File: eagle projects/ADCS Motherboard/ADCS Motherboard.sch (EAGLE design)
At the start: 140 parts, among them J1 HDR_10_EZFET_DEBUGGER, J11 CNC_3221-10-0300-00, J3 CNC_3221-10-0300-00, J5 CNC_3221-10-0300-00, J7 TE-1734829-3, J8 CNC_3221-10-0300-00, J9 CNC_3221-14-0300-00, Q1 PMV16XN, Q2 IRLML6246TRPBF, Q3 IRLML2246TRPBF, U1 MSP430F5529IPN, U2 LMV321, U3 ADS7841E_2K5, U4 LMV321, U5 LMV321, U7 HMC1053, Y1 32.768kHz, Y2 CSTCR4M00G15L99, Y3 32.768kHz

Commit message: Replaced connectors for Rev B
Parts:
- removed J8: CNC_3221-10-0300-00, my_library:CNC_3221-10-0300-00
- removed J9: CNC_3221-14-0300-00, my_library:CNC_3221-14-0300-00
- removed R56: 5.1M, rcl:R-US_R0603
- added JP2: (no value), pinhead:PINHD-2X12
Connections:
- removed net N$55: J8.9, R56.2
- removed net RW_X_OUTFG: J9.13, U1.P7.4/TB0.2
- removed net RW_Y_OUTFG: J8.1, U1.P5.7/TB0.1
- removed net RW_Z_OUTFG: J8.2, U1.P3.6/TB0.6
- new net N$1: JP2.24
- new net RW_X_LOCK: JP2.9
- new net RW_Y_LOCK: JP2.15
- new net RW_Z_LOCK: JP2.3
- net !CS!_CURR_SENSE_MTQR: now also JP2.23; no longer J8.5
- net !CS!_CURR_SENSE_RW: now also JP2.21; no longer J8.3
- net ACT_BRD_3V_PRESENT: no longer J8.7
- net ACT_BRD_5V_PRESENT: now also JP2.2; no longer J9.14
- net GND: no longer R56.1
- net MAG_X_FIN: now also JP2.8; no longer J9.10
- net MAG_X_RIN: now also JP2.6; no longer J9.12
- net MAG_Y_FIN: now also JP2.12; no longer J9.6
- net MAG_Y_RIN: now also JP2.10; no longer J9.8
- net MAG_Z_FIN: now also JP2.16; no longer J9.2
- net MAG_Z_RIN: now also JP2.14; no longer J9.4
- net N$57: now also JP2.4; no longer J8.10
- net RW_X_DIR: now also JP2.13; no longer J9.7
- net RW_X_SPEED_CTRL: now also JP2.11; no longer J9.1
- net RW_Y_DIR: now also JP2.19; no longer J9.9
- net RW_Y_SPEED_CTRL: now also JP2.17; no longer J9.3
- net RW_Z_DIR: now also JP2.7; no longer J9.11
- net RW_Z_SPEED_CTRL: now also JP2.5; no longer J9.5
- net UCB0_SPI_CLK: now also JP2.18; no longer J8.4
- net UCB0_SPI_MISO: now also JP2.22; no longer J8.6
- net UCB0_SPI_MOSI: now also JP2.20; no longer J8.8
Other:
- note removed: "PWM_IN"

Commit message: Ton of layout changes.. too many to count but this is rev b
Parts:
- removed JP1: (no value), my_library:PINHD-1X5
- removed R39, R40: 10k, rcl:R-US_R0402
- removed U5: LMV321, my_library:LMV321
- added C32, C33: 0.1uF, rcl:C-EUC0805
- added R57, R58: 5.1M, rcl:R-US_R0402
- added R59, R60: 4.7k, rcl:R-US_R0603
- added U10: TSV991AILT, my_library:TSV991AILT
- added U9: BMX160, my_library:BMX160
- J2, R48, U6, Y3: POPULATE (none) -> DNP
- R19: device rcl:R-US_R0805 -> rcl:R-US_R0402
- U2, U4: value LMV321 -> TSV991AILT; device my_library:LMV321 -> my_library:TSV991AILT
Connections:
- removed net N$57: JP2.4, R55.1
- removed net P1.0: JP1.1, U1.P1.0/TA0CLK/ACLK
- removed net P1.1: JP1.2, U1.P1.1/TA0.0
- removed net P2.3: JP1.3, U1.P2.3/TA2.0
- new net !CS!_SPD_SENSE_RW: JP2.24, U1.P3.6/TB0.6
- new net BMX160_INT1: U1.P2.3/TA2.0, U9.INT1
- new net BMX160_INT2: U9.INT2
- new net N$18: R58.1, U9.DNC_2
- new net N$19: R57.1, U9.DNC_1
- new net N$2: C32.1, U9.VDDIO
- new net N$41: U1.P3.7/TB0OUTH/SVMOUT
- net !CS!_CURR_SENSE_MTQR: now also U1.P5.7/TB0.1; no longer U1.P5.1/A9/VREF-/VEREF-
- net !CS!_CURR_SENSE_RW: now also U1.P7.4/TB0.2; no longer U1.P5.0/A8/VREF+/VEREF+
- net !CS!_HMC1053: now also U1.P7.1/CB9/A13; no longer U1.P2.7/UCB0STE/UCA0CLK
- net !CS!_SUN_X+: now also U1.PJ.2/TMS; no longer U1.P4.3/PM_UCB1CLK/PM_UCA1STE
- net !CS!_SUN_X-: now also U1.P6.0/CB0/A0; no longer U1.P8.0
- net !CS!_SUN_Y+: now also U1.P6.2/CB2/A2; no longer U1.P6.5/CB5/A5
- net !CS!_SUN_Y-: now also U1.P6.3/CB3/A3; no longer U1.P8.1
- net !CS!_SUN_Z+: now also U1.P6.1/CB1/A1; no longer U1.P6.6/CB6/A6
- net !CS!_SUN_Z-: now also U1.PJ.3/TCK; no longer U1.P8.2
- net +3V3: now also C33.1, R59.2, R60.2, U10.VCC, U2.VCC, U4.VCC, U9.VDD; no longer R39.2, R40.2, U2.V+, U4.V+, U5.V+
- net ACT_BRD_3V_PRESENT: now also JP2.1
- net BNO055_INT: now also U1.P2.2/TA2CLK/SMCLK; no longer U1.P1.6/TA1CLK/CBOUT
- net BNO055_RST: now also U1.P7.2/CB10/A14; no longer U1.P6.3/CB3/A3
- net B_MEAS_X: now also U2.OUT; no longer U4.OUT
- net B_MEAS_Y: now also U10.OUT; no longer U2.OUT
- net B_MEAS_Z: now also U4.OUT; no longer U5.OUT
- net GND: now also C32.2, C33.2, R55.1, R57.2, R58.2, U10.VSS, U2.VSS, U4.VSS, U9.CSB, U9.GNDIO, U9.GND_1, U9.GND_2, U9.GND_3, U9.SDO; no longer R55.2, U2.V-, U4.V-, U5.V-
- net HMC1053_RESET: now also U1.P6.5/CB5/A5; no longer U1.P6.4/CB4/A4
- net MAG_X_FIN: now also U1.P1.3/TA0.2; no longer U1.P1.2/TA0.1
- net MAG_X_RIN: now also U1.P1.2/TA0.1; no longer U1.P1.3/TA0.2
- net MAG_Y_FIN: now also U1.P1.5/TA0.4; no longer U1.P2.0/TA1.1
- net MAG_Y_RIN: now also U1.P1.4/TA0.3; no longer U1.P2.1/TA1.2
- net MAG_Z_FIN: now also U1.P2.1/TA1.2; no longer U1.P1.4/TA0.3
- net MAG_Z_RIN: now also U1.P2.0/TA1.1; no longer U1.P1.5/TA0.4
- net MSP430_ACTIVE: now also U1.P6.4/CB4/A4; no longer U1.P6.0/CB0/A0
- net N$1: now also JP2.4, R55.2; no longer JP2.24
- net N$21: now also U10.IN-; no longer U2.-
- net N$23: now also U10.IN+; no longer U2.+
- net N$50: now also U2.IN-; no longer U4.-
- net N$52: now also U2.IN+; no longer U4.+
- net N$60: now also U4.IN-; no longer U5.-
- net N$62: now also U4.IN+; no longer U5.+
- net RESERVED_1: now also U1.P2.6/RTCCLK/DMAE0; no longer U1.P2.2/TA2CLK/SMCLK
- net RESERVED_2: now also U1.P2.7/UCB0STE/UCA0CLK; no longer U1.P2.6/RTCCLK/DMAE0
- net RW_X_DIR: now also U1.P4.6/PM_NONE; no longer U1.PJ.3/TCK
- net RW_X_LOCK: now also U1.P1.0/TA0CLK/ACLK
- net RW_Y_DIR: now also U1.P4.7/PM_NONE; no longer U1.PJ.2/TMS
- net RW_Y_LOCK: now also U1.P1.1/TA0.0
- net RW_Z_DIR: now also U1.P5.6/TB0.0; no longer U1.PJ.1/TDI/TCLK
- net RW_Z_LOCK: now also U1.P1.6/TA1CLK/CBOUT
- net TB0.3: no longer JP1.4
- net TB0.4: no longer JP1.5
- net UCB1_I2C_SCL: now also R60.1, U9.SCX; no longer R40.1
- net UCB1_I2C_SDA: now also R59.1, U9.SDX; no longer R39.1
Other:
- note added: "BMX160_INT2"
- note added: "COMPONENTS NOT POPULATED ON REV B DUE TO CHIP SHORTAGE"
- note added: "CSB is I2C/SPI mode select pin Set to GND is I2C mode"
- note added: "SDO is address select pin Set to GND address = 0x68"
- note removed: "was !CS!_SUN_Y+"
- note removed: "was !CS!_SUN_Z+"
- moved on the sheet: C24, C25, C26, C27, C28, J2, JP2, LED2, LED3, R30, R31, R32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

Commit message: Rev B almost ready
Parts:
- removed J3: CNC_3221-10-0300-00, my_library:CNC_3221-10-0300-00
- added JP1: (no value), pinhead:PINHD-2X5
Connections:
- net !CS!_SUN_X+: now also JP1.2; no longer J3.2
- net !CS!_SUN_X-: now also JP1.7; no longer J3.7
- net !CS!_SUN_Y+: now also JP1.4; no longer J3.4
- net !CS!_SUN_Y-: now also JP1.9; no longer J3.9
- net !CS!_SUN_Z-: now also JP1.6; no longer J3.6
- net N$58: now also JP1.8; no longer J3.8
- net UCB0_SPI_CLK: now also JP1.5; no longer J3.5
- net UCB0_SPI_MISO: now also JP1.1; no longer J3.1
- net UCB0_SPI_MOSI: now also JP1.3; no longer J3.3
- net Z-_SUN_3V_PRESENT: now also JP1.10; no longer J3.10
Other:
- moved on the sheet: JP4, R45

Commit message: Idk what i changed
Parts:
- Q1: value PMV16XN -> BSR802NL6327HTSA1; device my_library:PMV16XN -> my_library:BSR802NL6327HTSA1
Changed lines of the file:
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@@
 <part name="R36" library="rcl" library_urn="urn:adsk.eagle:library:334" deviceset="R-US_" device="R0603" package3d_urn="urn:adsk.eagle:package:23555/3" value="10k"/>
 <part name="SUPPLY26" library="supply2" library_urn="urn:adsk.eagle:library:372" deviceset="GND" device=""/>
-<part name="Q1" library="my_library" library_urn="urn:adsk.eagle:library:22876504" deviceset="PMV16XN" device="" package3d_urn="urn:adsk.eagle:package:24628515/1"/>
+<part name="Q1" library="my_library" library_urn="urn:adsk.eagle:library:22876504" deviceset="BSR802NL6327HTSA1" device="" package3d_urn="urn:adsk.eagle:package:24628515/1"/>
 <part name="Q3" library="my_library" library_urn="urn:adsk.eagle:library:22876504" deviceset="IRLML2246TRPBF" device="" package3d_urn="urn:adsk.eagle:package:24628516/1"/>
 <part name="Q2" library="my_library" library_urn="urn:adsk.eagle:library:22876504" deviceset="IRLML6246TRPBF" device="" package3d_urn="urn:adsk.eagle:package:24628516/1"/>
@@
 </instance>
 <instance part="Q1" gate="G$1" x="241.3" y="162.56" smashed="yes" rot="MR0">
-<attribute name="VALUE" x="232.41" y="161.29" size="1.778" layer="96" rot="MR0"/>
-<attribute name="NAME" x="232.41" y="163.83" size="1.778" layer="95" rot="MR0"/>
+<attribute name="VALUE" x="245.11" y="166.37" size="1.778" layer="96" rot="MR180"/>
+<attribute name="NAME" x="245.11" y="168.91" size="1.778" layer="95" rot="MR180"/>
 </instance>
 <instance part="FRAME1" gate="G$1" x="0" y="0" smashed="yes"/>
@@
 <wire x1="218.44" y1="170.18" x2="238.76" y2="170.18" width="0.1524" layer="91"/>
 <pinref part="R7" gate="G$1" pin="1"/>
-<wire x1="238.76" y1="170.18" x2="248.92" y2="170.18" width="0.1524" layer="91"/>
 <wire x1="218.44" y1="170.18" x2="218.44" y2="172.72" width="0.1524" layer="91"/>
 <junction x="218.44" y="170.18"/>
@@
 <junction x="218.44" y="160.02"/>
 <wire x1="218.44" y1="160.02" x2="210.82" y2="160.02" width="0.1524" layer="91"/>
-<label x="248.92" y="170.18" size="1.778" layer="95" rot="MR180" xref="yes"/>
+<label x="248.92" y="175.26" size="1.778" layer="95" rot="MR180" xref="yes"/>
 <pinref part="S1" gate="1" pin="S1"/>
 <wire x1="208.28" y1="160.02" x2="210.82" y2="160.02" width="0.1524" layer="91"/>
@@
 <pinref part="Q1" gate="G$1" pin="D"/>
 <junction x="238.76" y="170.18"/>
-</segment>
-</net>
+<wire x1="238.76" y1="170.18" x2="238.76" y2="175.26" width="0.1524" layer="91"/>
+<wire x1="238.76" y1="175.26" x2="248.92" y2="175.26" width="0.1524" layer="91"/>
+</segment>
+</net>

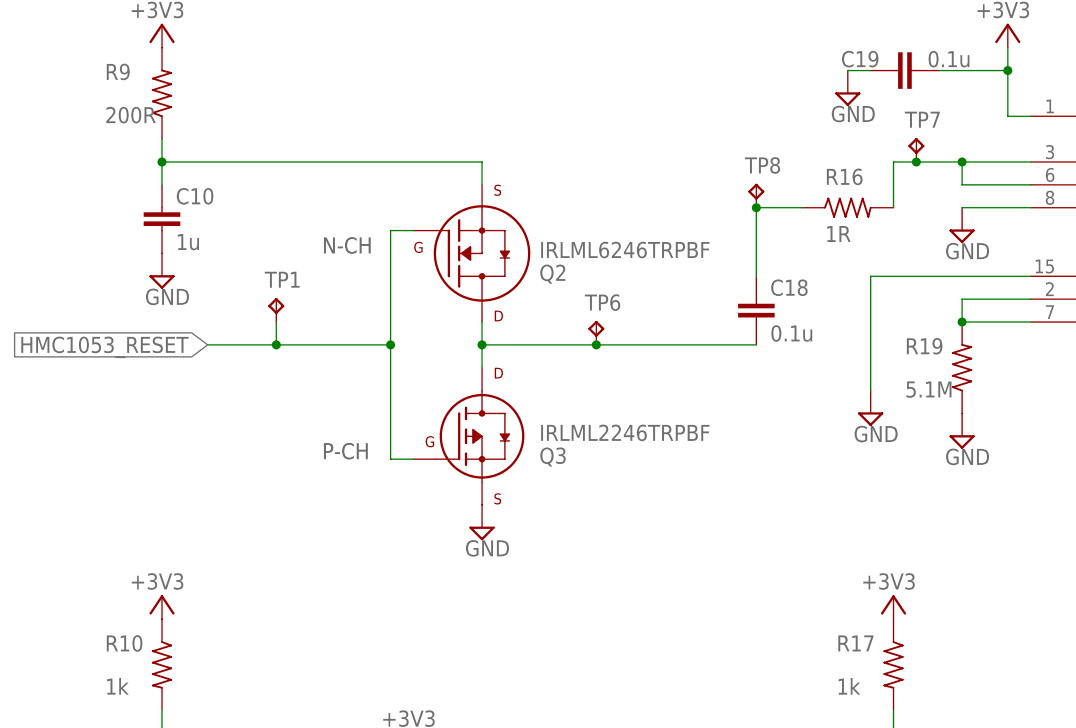
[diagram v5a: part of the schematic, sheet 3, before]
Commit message: Replace totem pole driver with complementary Mosfets pair package
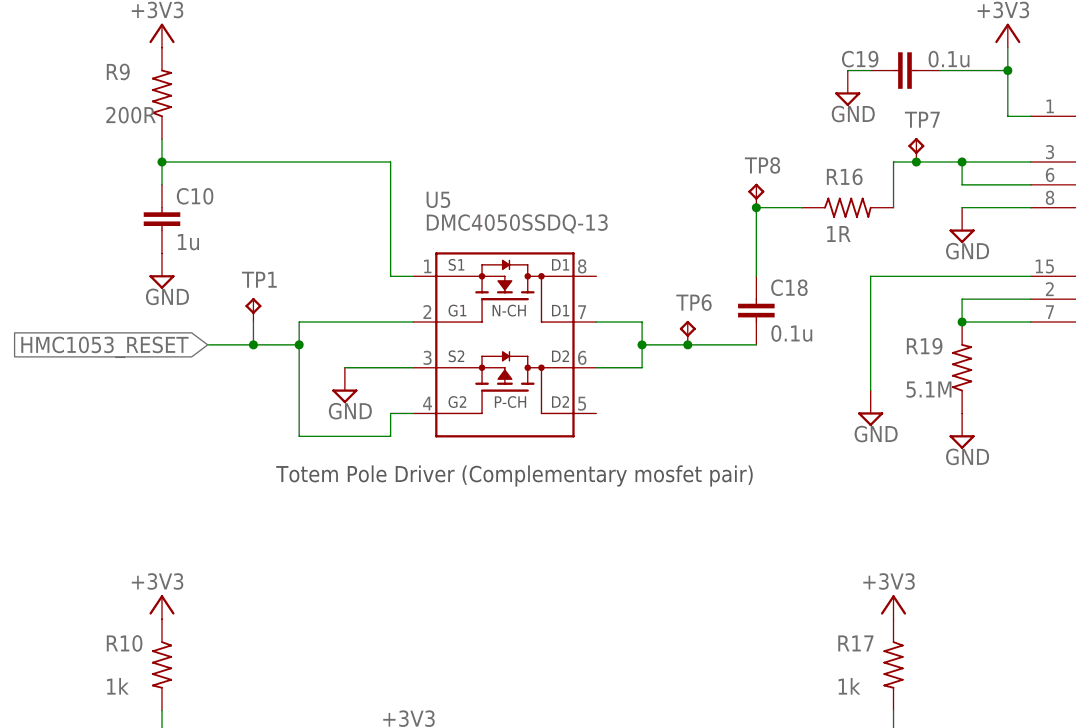
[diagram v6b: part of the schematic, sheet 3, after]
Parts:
- removed Q2: IRLML6246TRPBF, my_library:IRLML6246TRPBF
- removed Q3: IRLML2246TRPBF, my_library:IRLML2246TRPBF
- added U5: DMC4050SSDQ-13, my_library:DMC4050SSDQ-13
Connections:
- net GND: now also U5.S2; no longer Q3.S
- net HMC1053_RESET: now also U5.G1, U5.G2; no longer Q2.G, Q3.G
- net N$39: now also U5.S1; no longer Q2.S
- net N$9: now also U5.D1_2, U5.D2_1; no longer Q2.D, Q3.D
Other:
- note added: "Totem Pole Driver (Complementary mosfet pair)"
- note removed: "N-CH"
- note removed: "P-CH"
- moved on the sheet: TP1, TP6
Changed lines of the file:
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@@
 <part name="SUPPLY26" library="supply2" library_urn="urn:adsk.eagle:library:372" deviceset="GND" device=""/>
 <part name="Q1" library="my_library" library_urn="urn:adsk.eagle:library:22876504" deviceset="BSR802NL6327HTSA1" device="" package3d_urn="urn:adsk.eagle:package:24628515/1"/>
-<part name="Q3" library="my_library" library_urn="urn:adsk.eagle:library:22876504" deviceset="IRLML2246TRPBF" device="" package3d_urn="urn:adsk.eagle:package:24628516/1"/>
-<part name="Q2" library="my_library" library_urn="urn:adsk.eagle:library:22876504" deviceset="IRLML6246TRPBF" device="" package3d_urn="urn:adsk.eagle:package:24628516/1"/>
 <part name="+3V2" library="supply1" deviceset="+3V3" device=""/>
 <part name="J4" library="my_library" library_urn="urn:adsk.eagle:library:22876504" deviceset="HDR_1X2" device="_" package3d_urn="urn:adsk.eagle:package:24527019/1"/>
@@
 <part name="U4" library="my_library" library_urn="urn:adsk.eagle:library:22876504" deviceset="TSV991AILT" device="" package3d_urn="urn:adsk.eagle:package:24426275/2"/>
 <part name="JP1" library="pinhead" library_urn="urn:adsk.eagle:library:325" deviceset="PINHD-2X5" device="" package3d_urn="urn:adsk.eagle:package:22470/2"/>
+<part name="U5" library="my_library" library_urn="urn:adsk.eagle:library:22876504" deviceset="DMC4050SSDQ-13" device=""/>
 </parts>
 <sheets>
@@
 BUSY - Output high impedance when !CS! is HIGH</text>
 <text x="119.38" y="17.78" size="1.778" layer="97">NC</text>
-<text x="45.72" y="154.94" size="1.778" layer="97">P-CH</text>
-<text x="45.72" y="177.8" size="1.778" layer="97">N-CH</text>
 <text x="261.62" y="7.62" size="2.54" layer="94">A.1</text>
+<text x="40.64" y="152.4" size="1.778" layer="97">Totem Pole Driver (Complementary mosfet pair)</text>
 </plain>
 <instances>
@@
 <attribute name="VALUE" x="102.235" y="192.405" size="1.778" layer="96"/>
 </instance>
-<instance part="SUPPLY54" gate="GND" x="63.5" y="147.32" smashed="yes">
-<attribute name="VALUE" x="61.595" y="144.145" size="1.778" layer="96"/>
+<instance part="SUPPLY54" gate="GND" x="48.26" y="162.56" smashed="yes">
+<attribute name="VALUE" x="46.355" y="159.385" size="1.778" layer="96"/>
 </instance>
 <instance part="+3V24" gate="G$1" x="27.94" y="203.2" smashed="yes">
@@
 <attribute name="VALUE" x="199.39" y="113.538" size="1.778" layer="96"/>
 </instance>
-<instance part="TP1" gate="G$1" x="40.64" y="172.72" smashed="yes">
-<attribute name="NAME" x="39.37" y="173.99" size="1.778" layer="95"/>
+<instance part="TP1" gate="G$1" x="38.1" y="172.72" smashed="yes">
+<attribute name="NAME" x="36.83" y="173.99" size="1.778" layer="95"/>
 </instance>
 <instance part="TP2" gate="G$1" x="147.32" y="43.18" smashed="yes">
 <attribute name="NAME" x="146.05" y="44.45" size="1.778" layer="95"/>
-</instance>
-<instance part="Q3" gate="G$1" x="60.96" y="157.48" smashed="yes" rot="MR180">
-<attribute name="VALUE" x="69.85" y="158.75" size="1.778" layer="96" rot="MR180"/>
-<attribute name="NAME" x="69.85" y="156.21" size="1.778" layer="95" rot="MR180"/>
-</instance>
-<instance part="Q2" gate="G$1" x="60.96" y="177.8" smashed="yes" rot="MR180">
-<attribute name="VALUE" x="69.85" y="179.07" size="1.778" layer="96" rot="MR180"/>
-<attribute name="NAME" x="69.85" y="176.53" size="1.778" layer="95" rot="MR180"/>
 </instance>
 <instance part="FRAME2" gate="G$1" x="0" y="0" smashed="yes"/>
@@
 <attribute name="VALUE" x="104.775" y="156.845" size="1.778" layer="96"/>
 </instance>
-<instance part="TP6" gate="G$1" x="76.2" y="170.18" smashed="yes">
-<attribute name="NAME" x="74.93" y="171.45" size="1.778" layer="95"/>
+<instance part="TP6" gate="G$1" x="86.36" y="170.18" smashed="yes">
+<attribute name="NAME" x="85.09" y="171.45" size="1.778" layer="95"/>
 </instance>
 <instance part="TP7" gate="G$1" x="111.76" y="190.5" smashed="yes">
@@
 <attribute name="NAME" x="226.06" y="102.87" size="1.27" layer="95"/>
 <attribute name="VALUE" x="226.06" y="100.33" size="1.27" layer="96"/>
+</instance>
+<instance part="U5" gate="G$1" x="63.5" y="167.64" smashed="yes">
+<attribute name="VALUE" x="57.15" y="180.34" size="1.778" layer="96"/>
+<attribute name="NAME" x="57.15" y="182.88" size="1.778" layer="95"/>
 </instance>
 </instances>
@@
 </segment>
 <segment>
-<pinref part="SUPPLY54" gate="GND" pin="GND"/>
-<pinref part="Q3" gate="G$1" pin="S"/>
-</segment>
-<segment>
 <pinref part="C29" gate="G$1" pin="2"/>
 <pinref part="SUPPLY40" gate="GND" pin="GND"/>
@@
 <pinref part="SUPPLY34" gate="GND" pin="GND"/>
 <wire x1="220.98" y1="86.36" x2="220.98" y2="83.82" width="0.1524" layer="91"/>
+</segment>
+<segment>
+<pinref part="U5" gate="G$1" pin="S2"/>
+<pinref part="SUPPLY54" gate="GND" pin="GND"/>
+<wire x1="55.88" y1="165.1" x2="48.26" y2="165.1" width="0.1524" layer="91"/>
 </segment>
 </net>
@@
 <net name="HMC1053_RESET" class="0">
 <segment>
-<wire x1="53.34" y1="167.64" x2="40.64" y2="167.64" width="0.1524" layer="91"/>
-<wire x1="40.64" y1="170.18" x2="40.64" y2="167.64" width="0.1524" layer="91"/>
-<junction x="40.64" y="167.64"/>
-<wire x1="40.64" y1="167.64" x2="33.02" y2="167.64" width="0.1524" layer="91"/>
+<wire x1="43.18" y1="167.64" x2="38.1" y2="167.64" width="0.1524" layer="91"/>
+<wire x1="38.1" y1="170.18" x2="38.1" y2="167.64" width="0.1524" layer="91"/>
+<junction x="38.1" y="167.64"/>
+<wire x1="38.1" y1="167.64" x2="33.02" y2="167.64" width="0.1524" layer="91"/>
 <label x="33.02" y="167.64" size="1.778" layer="95" rot="R180" xref="yes"/>
 <pinref part="TP1" gate="G$1" pin="TP"/>
-<pinref part="Q3" gate="G$1" pin="G"/>
-<wire x1="55.88" y1="154.94" x2="53.34" y2="154.94" width="0.1524" layer="91"/>
-<pinref part="Q2" gate="G$1" pin="G"/>
-<wire x1="53.34" y1="154.94" x2="53.34" y2="167.64" width="0.1524" layer="91"/>
-<wire x1="53.34" y1="167.64" x2="53.34" y2="180.34" width="0.1524" layer="91"/>
-<wire x1="53.34" y1="180.34" x2="55.88" y2="180.34" width="0.1524" layer="91"/>
-<junction x="53.34" y="167.64"/>
+<pinref part="U5" gate="G$1" pin="G2"/>
+<wire x1="55.88" y1="160.02" x2="53.34" y2="160.02" width="0.1524" layer="91"/>
+<wire x1="43.18" y1="157.48" x2="43.18" y2="167.64" width="0.1524" layer="91"/>
+<junction x="43.18" y="167.64"/>
+<wire x1="43.18" y1="167.64" x2="43.18" y2="170.18" width="0.1524" layer="91"/>
+<pinref part="U5" gate="G$1" pin="G1"/>
+<wire x1="43.18" y1="170.18" x2="55.88" y2="170.18" width="0.1524" layer="91"/>
+<wire x1="43.18" y1="157.48" x2="53.34" y2="157.48" width="0.1524" layer="91"/>
+<wire x1="53.34" y1="157.48" x2="53.34" y2="160.02" width="0.1524" layer="91"/>
 </segment>
 </net>
@@
 <wire x1="27.94" y1="185.42" x2="27.94" y2="187.96" width="0.1524" layer="91"/>
 <wire x1="27.94" y1="187.96" x2="27.94" y2="190.5" width="0.1524" layer="91"/>
-<wire x1="63.5" y1="187.96" x2="27.94" y2="187.96" width="0.1524" layer="91"/>
 <junction x="27.94" y="187.96"/>
-<pinref part="Q2" gate="G$1" pin="S"/>
-<wire x1="63.5" y1="185.42" x2="63.5" y2="187.96" width="0.1524" layer="91"/>
+<wire x1="53.34" y1="187.96" x2="27.94" y2="187.96" width="0.1524" layer="91"/>
+<pinref part="U5" gate="G$1" pin="S1"/>
+<wire x1="55.88" y1="175.26" x2="53.34" y2="175.26" width="0.1524" layer="91"/>
+<wire x1="53.34" y1="175.26" x2="53.34" y2="187.96" width="0.1524" layer="91"/>
 </segment>
 </net>
@@
 <net name="N$9" class="0">
 <segment>
-<pinref part="Q2" gate="G$1" pin="D"/>
-<pinref part="Q3" gate="G$1" pin="D"/>
-<wire x1="63.5" y1="170.18" x2="63.5" y2="167.64" width="0.1524" layer="91"/>
-<wire x1="63.5" y1="167.64" x2="63.5" y2="165.1" width="0.1524" layer="91"/>
-<wire x1="63.5" y1="167.64" x2="76.2" y2="167.64" width="0.1524" layer="91"/>
-<junction x="63.5" y="167.64"/>
 <pinref part="C18" gate="G$1" pin="1"/>
 <pinref part="TP6" gate="G$1" pin="TP"/>
-<wire x1="76.2" y1="167.64" x2="93.98" y2="167.64" width="0.1524" layer="91"/>
-<junction x="76.2" y="167.64"/>
-</segment>
-</net>
+<wire x1="86.36" y1="167.64" x2="93.98" y2="167.64" width="0.1524" layer="91"/>
+<pinref part="U5" gate="G$1" pin="D1_2"/>
+<wire x1="76.2" y1="170.18" x2="81.28" y2="170.18" width="0.1524" layer="91"/>
+<wire x1="81.28" y1="170.18" x2="81.28" y2="167.64" width="0.1524" layer="91"/>
+<wire x1="81.28" y1="167.64" x2="86.36" y2="167.64" width="0.1524" layer="91"/>
+<junction x="86.36" y="167.64"/>
+<wire x1="81.28" y1="167.64" x2="81.28" y2="165.1" width="0.1524" layer="91"/>
+<junction x="81.28" y="167.64"/>
+<pinref part="U5" gate="G$1" pin="D2_1"/>
+<wire x1="81.28" y1="165.1" x2="76.2" y2="165.1" width="0.1524" layer="91"/>
+</segment>
+</net>
